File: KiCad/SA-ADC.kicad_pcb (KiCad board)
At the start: 2 copper layers, 95.9 x 69.2 mm, 190 parts, among them J1 Conn_01x03, J2 Conn_01x02, J3 Conn_01x08, SW1 SW_Push_SPDT, SW2 SW_Push, U1 74LVC1G04, U10 74LVC1G32, U11 74LVC1G32, U12 74LVC1G32, U13 74LVC1G32, U14 74LVC1G32, U15 74LVC1G32, U16 74LVC1G32, U17 74LVC1G157, U18 74LVC1G157, U19 74LVC1G157, U2 74LVC1G08, U20 74LVC1G157, U21 74LVC1G157, U22 74LVC1G157, U23 74LVC1G157, U24 74LS377, U25 74LVC1G04, U26 74LS377, U27 74LVC1G04, U28 74HC164, U29 74LVC1G175, U3 74LVC1G32, U30 74HC02, U31 74HC02, U34 LM358, U35 74LVC1G125, U37 LM317L_TO92, U38 L7805, U4 74HC245, U44 LM555, U45 74LVC1G125, U47 74LVC1G32, U48 74LVC1G125, U5 74LVC1G32, U6 74LVC1G32, U7 74LVC1G32, U8 74LVC1G32, U9 74LVC1G32

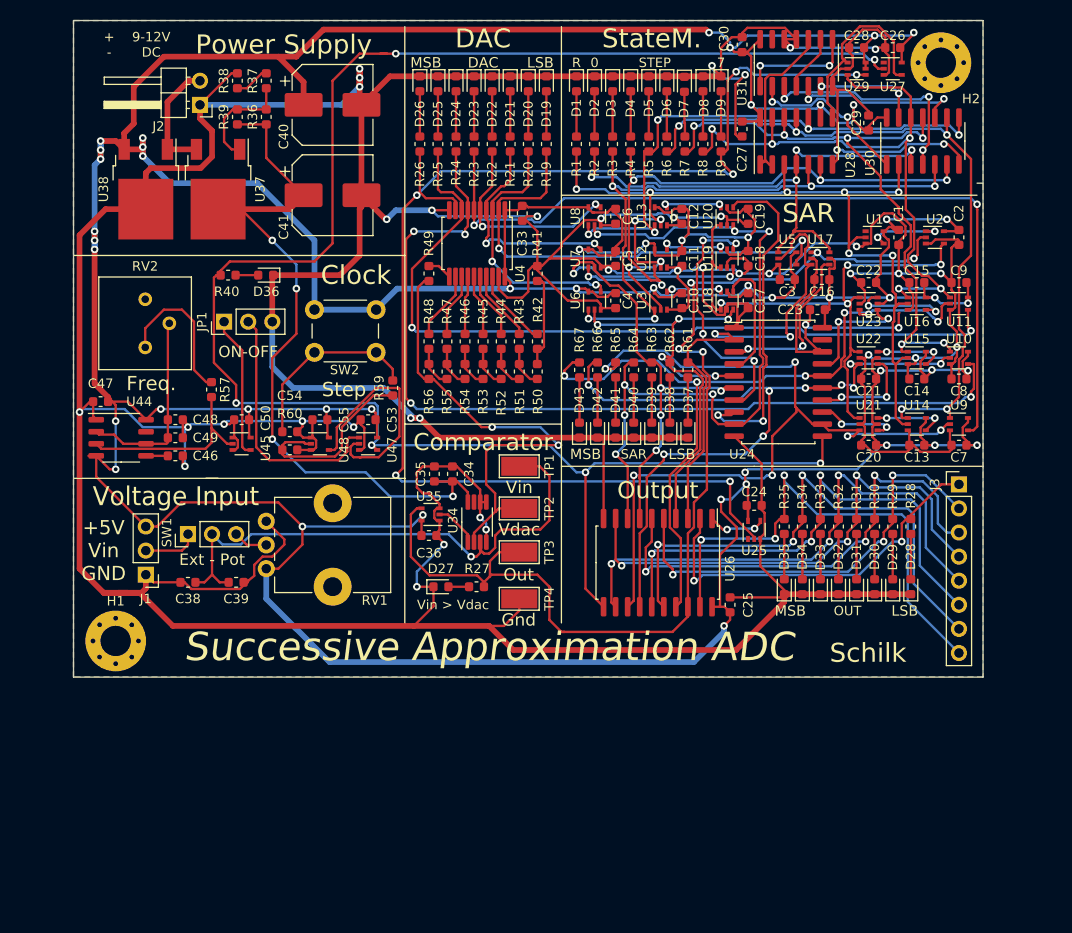
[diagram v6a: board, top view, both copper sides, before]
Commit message: Fixed State Numbering/Wiring Order
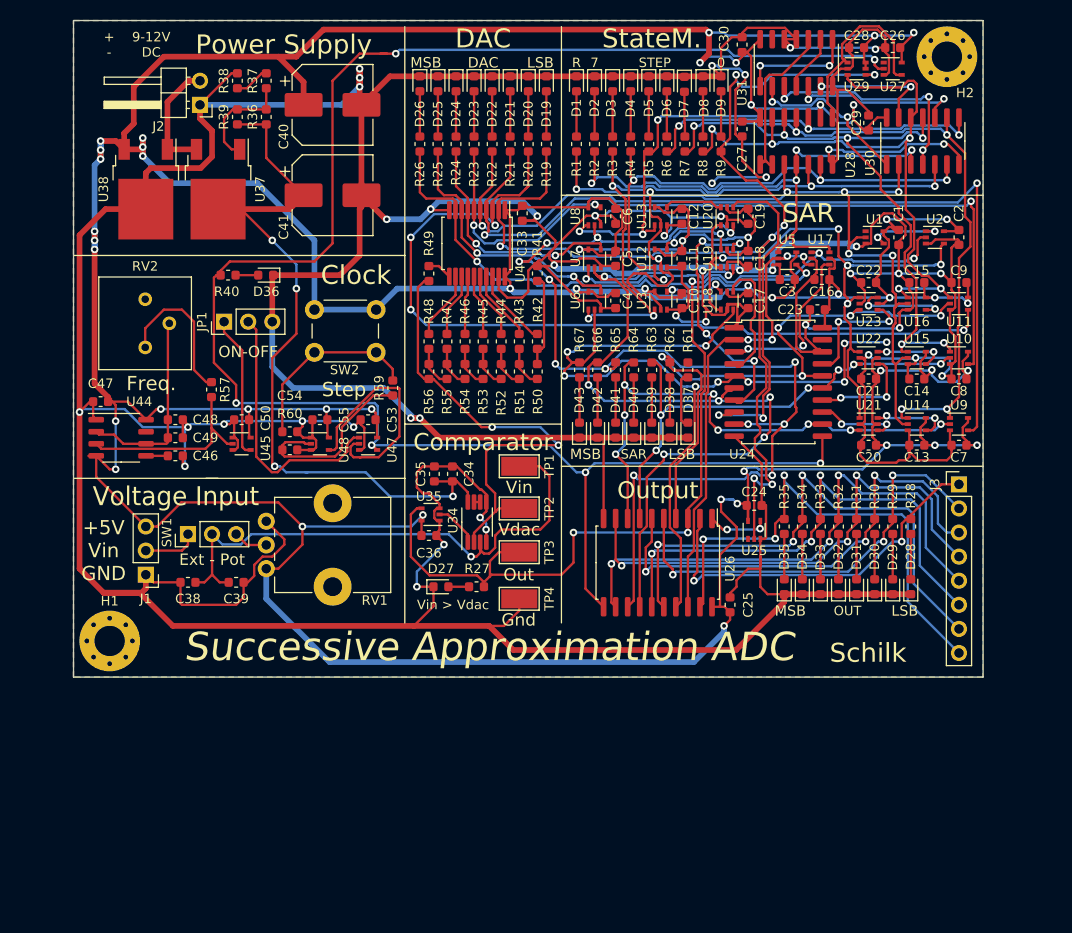
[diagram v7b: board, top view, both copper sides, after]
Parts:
- C48: value 200nf -> 0u1
- R57: value 10K -> 5K6
- RV2: value 5Meg -> 1Meg
- moved H2 0.90 mm to (186.7, 50.2)
- moved H1 0.64 mm to (98.4, 111.8)
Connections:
- net /SA-Register.sch/STATE0 renamed /SA-Register.sch/STATE7
- R3 pad 2: /SA-Register.sch/STATE1 -> /SA-Register.sch/STATE6
- R4 pad 2: /SA-Register.sch/STATE2 -> /SA-Register.sch/STATE5
- R5 pad 2: /SA-Register.sch/STATE3 -> /SA-Register.sch/STATE4
- R6 pad 2: /SA-Register.sch/STATE4 -> /SA-Register.sch/STATE3
- R61 pad 2: /Output/OUT_0 -> /SA-Register.sch/Q0
- R7 pad 2: /SA-Register.sch/STATE5 -> /SA-Register.sch/STATE2
- R8 pad 2: /SA-Register.sch/STATE6 -> /SA-Register.sch/STATE1
- R9 pad 2: /Analog/D7 -> /Analog/D0
- U10 pad 1: /SA-Register.sch/STATE5 -> /SA-Register.sch/STATE2
- U10 pad 2: /Output/OUT_5 -> /Output/OUT_2
- U10 pad 4: /Analog/D5 -> /Analog/D2
- U11 pad 1: /SA-Register.sch/STATE6 -> /SA-Register.sch/STATE1
- U11 pad 2: /Output/OUT_6 -> /Output/OUT_1
- U11 pad 4: /Analog/D6 -> /Analog/D1
- U12 pad 1: /SA-Register.sch/STATE2 -> /SA-Register.sch/STATE5
- U13 pad 1: /SA-Register.sch/STATE3 -> /SA-Register.sch/STATE4
- U14 pad 1: /SA-Register.sch/STATE4 -> /SA-Register.sch/STATE3
- U15 pad 1: /SA-Register.sch/STATE5 -> /SA-Register.sch/STATE2
- U16 pad 1: /SA-Register.sch/STATE6 -> /SA-Register.sch/STATE1
- U17 pad 3: /Output/OUT_0 -> /Output/OUT_7
- U18 pad 3: /Output/OUT_1 -> /Output/OUT_6
- U19 pad 3: /Output/OUT_2 -> /Output/OUT_5
- U20 pad 3: /Output/OUT_3 -> /Output/OUT_4
- U21 pad 3: /Output/OUT_4 -> /Output/OUT_3
- U22 pad 3: /Output/OUT_5 -> /Output/OUT_2
- U23 pad 3: /Output/OUT_6 -> /Output/OUT_1
- U24 pad 12: /Output/OUT_4 -> /Output/OUT_3
- U24 pad 15: /Output/OUT_5 -> /Output/OUT_2
- U24 pad 16: /Output/OUT_6 -> /Output/OUT_1
- U24 pad 2: /Output/OUT_0 -> /Output/OUT_7
- U24 pad 5: /Output/OUT_1 -> /Output/OUT_6
- U24 pad 6: /Output/OUT_2 -> /Output/OUT_5
- U24 pad 9: /Output/OUT_3 -> /Output/OUT_4
- U25 pad 2: /Analog/D7 -> /Analog/D0
- U26 pad 18: /Analog/COMP_OUT -> /Output/OUT_7
- U26 pad 3: /Output/OUT_0 -> /Analog/COMP_OUT
- U28 pad 10: /SA-Register.sch/STATE3 -> /SA-Register.sch/STATE4
- U28 pad 11: /SA-Register.sch/STATE4 -> /SA-Register.sch/STATE3
- U28 pad 12: /SA-Register.sch/STATE5 -> /SA-Register.sch/STATE2
- U28 pad 13: /SA-Register.sch/STATE6 -> /SA-Register.sch/STATE1
- U28 pad 5: /SA-Register.sch/STATE1 -> /SA-Register.sch/STATE6
- U28 pad 6: /SA-Register.sch/STATE2 -> /SA-Register.sch/STATE5
- U29 pad 3: /SA-Register.sch/STATE6 -> /SA-Register.sch/STATE1
- U29 pad 4: /Analog/D7 -> /Analog/D0
- U3 pad 1: /SA-Register.sch/STATE1 -> /SA-Register.sch/STATE6
- U30 pad 11: /SA-Register.sch/STATE5 -> /SA-Register.sch/STATE2
- U30 pad 12: /SA-Register.sch/STATE6 -> /SA-Register.sch/STATE1
- U30 pad 5: /SA-Register.sch/STATE1 -> /SA-Register.sch/STATE6
- U30 pad 6: /SA-Register.sch/STATE2 -> /SA-Register.sch/STATE5
- U30 pad 8: /SA-Register.sch/STATE3 -> /SA-Register.sch/STATE4
- U30 pad 9: /SA-Register.sch/STATE4 -> /SA-Register.sch/STATE3
- U34 pad 6: GND -> Net-(U34-Pad6)
- U34 pad 7: Net-(U34-Pad7) -> Net-(U34-Pad6)
- U5 pad 2: /Output/OUT_0 -> /Output/OUT_7
- U5 pad 4: /Analog/D0 -> /Analog/D7
- U6 pad 1: /SA-Register.sch/STATE1 -> /SA-Register.sch/STATE6
- U6 pad 2: /Output/OUT_1 -> /Output/OUT_6
- U6 pad 4: /Analog/D1 -> /Analog/D6
- U7 pad 1: /SA-Register.sch/STATE2 -> /SA-Register.sch/STATE5
- U7 pad 2: /Output/OUT_2 -> /Output/OUT_5
- U7 pad 4: /Analog/D2 -> /Analog/D5
- U8 pad 1: /SA-Register.sch/STATE3 -> /SA-Register.sch/STATE4
- U8 pad 2: /Output/OUT_3 -> /Output/OUT_4
- U8 pad 4: /Analog/D3 -> /Analog/D4
- U9 pad 1: /SA-Register.sch/STATE4 -> /SA-Register.sch/STATE3
- U9 pad 2: /Output/OUT_4 -> /Output/OUT_3
- U9 pad 4: /Analog/D4 -> /Analog/D3
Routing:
- net /Analog/D7: track 143.8 -> 55.2 mm, vias 6 -> 2
- net /Analog/D5: track 97.6 -> 25.7 mm, vias 4 -> 2
- net /Analog/D0: track 50.6 -> 120.6 mm, vias 2 -> 7
- net /Analog/D3: track 22.2 -> 90.4 mm
- net /Analog/D1: track 28.0 -> 91.0 mm, vias 2 -> 4
- net /Analog/D4: track 87.1 -> 24.3 mm
- net /Analog/D2: track 23.8 -> 81.3 mm
- net /Analog/D6: track 84.6 -> 28.2 mm
- net /Output/OUT_0: track 52.8 -> 0.00 mm, vias 2 -> 0
- net /Output/OUT_7: track 0.00 -> 48.9 mm, vias 0 -> 4
- net GND: track 835.2 -> 882.2 mm, vias 41 -> 44
- net /Output/OUT_4: track 85.8 -> 116.6 mm, vias 6 -> 12
- net +5V: track 659.7 -> 688.0 mm
- net /SA-Register.sch/STATE3: track 58.6 -> 75.5 mm
- net /SA-Register.sch/STATE4: track 76.0 -> 59.4 mm
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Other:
- board text added: "v0.1"
- board text removed: "[version]"
